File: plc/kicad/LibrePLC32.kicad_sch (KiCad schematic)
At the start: 0 parts

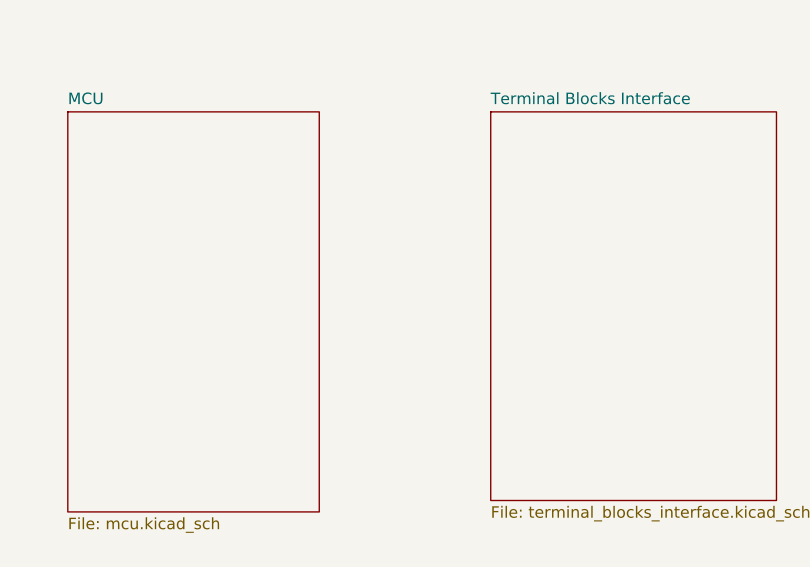
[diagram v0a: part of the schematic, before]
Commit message: Added gpio multiplexer and relay circuit
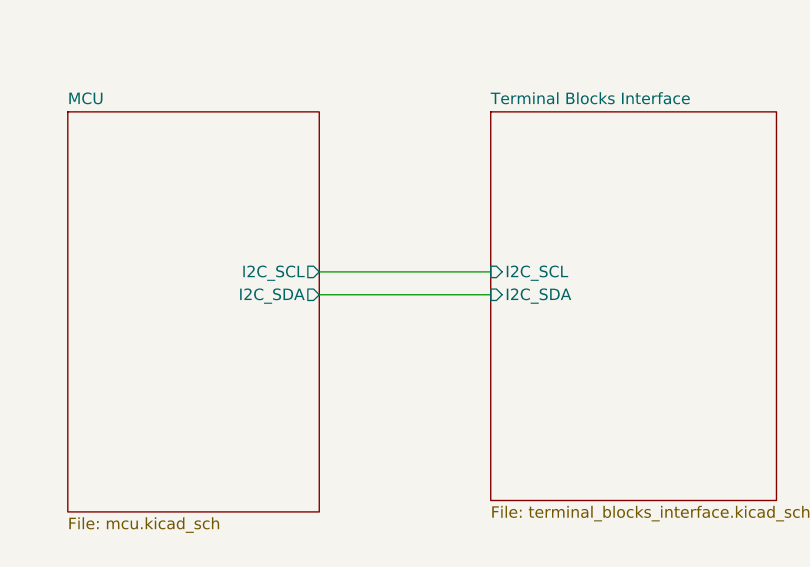
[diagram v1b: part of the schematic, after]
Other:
- sheet MCU ports: added I2C_SCL, I2C_SDA; removed none
- sheet Terminal Blocks Interface ports: added I2C_SCL, I2C_SDA; removed none
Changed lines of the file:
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@@
 	(generator_version "10.0")
 	(paper "A4")
+	(wire
+		(pts
+			(xy 154.94 90.17) (xy 173.99 90.17)
+		)
+		(stroke
+			(width 0)
+			(type default)
+		)
+	)
+	(wire
+		(pts
+			(xy 154.94 87.63) (xy 173.99 87.63)
+		)
+		(stroke
+			(width 0)
+			(type default)
+		)
+	)
 	(sheet
 		(at 50.8 74.93)
@@
 			)
 		)
+		(pin "I2C_SDA" input
+			(at 173.99 90.17 180)
+			(effects
+				(font
+					(size 1.27 1.27)
+				)
+				(justify left)
+			)
+		)
+		(pin "I2C_SCL" input
+			(at 173.99 87.63 180)
+			(effects
+				(font
+					(size 1.27 1.27)
+				)
+				(justify left)
+			)
+		)
 		(instances
 			(project "LibrePLC32"
@@
 			)
 		)
+		(pin "I2C_SDA" output
+			(at 154.94 90.17 0)
+			(effects
+				(font
+					(size 1.27 1.27)
+				)
+				(justify right)
+			)
+		)
+		(pin "I2C_SCL" output
+			(at 154.94 87.63 0)
+			(effects
+				(font
+					(size 1.27 1.27)
+				)
+				(justify right)
+			)
+		)

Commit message: Updated ethernet circuit
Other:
- sheet Ethernet ports: added ETH_MISO, ETH_MOSI, ETH_SCLK, ~{ETH_CS}, ~{ETH_INT}, ~{ETH_RST}; removed none
- sheet MCU ports: added ADC_RDY, ETH_MISO, ETH_MOSI, ETH_SCLK, MCU_DI, ~{ETH_CS}, ~{ETH_INT}, ~{ETH_RST}, ~{MUX_INT}; removed none
- sheet Terminal Blocks Interface ports: added ADC_RDY, MCU_DI, ~{MUX_INT}; removed none

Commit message: Added RS 485 circuit
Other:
- sheet MCU ports: added RS485_DIR, RS485_RXD, RS485_TXD; removed none
- sheet RS-485 ports: added RS485_DIR, RS485_RXD, RS485_TXD; removed none
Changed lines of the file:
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@@
+	(wire
+		(pts
+			(xy 127 102.235) (xy 82.55 102.235)
+		)
+		(stroke
+			(width 0)
+			(type default)
+		)
+	)
 	(wire
 		(pts
@@
 	(wire
 		(pts
+			(xy 82.55 104.775) (xy 127 104.775)
+		)
+		(stroke
+			(width 0)
+			(type default)
+		)
+	)
+	(wire
+		(pts
 			(xy 218.44 102.235) (xy 178.435 102.235)
+		)
+		(stroke
+			(width 0)
+			(type default)
+		)
+	)
+	(wire
+		(pts
+			(xy 82.55 107.315) (xy 127 107.315)
 		)
 		(stroke
@@
 	)
 	(sheet
-		(at 50.8 99.06)
-		(size 31.75 12.7)
+		(at 50.8 97.79)
+		(size 31.75 14.605)
 		(exclude_from_sim no)
 		(in_bom yes)
@@
 		)
 		(property "Sheetname" "RS-485"
-			(at 50.8 98.3484 0)
+			(at 50.8 97.0784 0)
 			(show_name no)
 			(do_not_autoplace no)
@@
 		)
 		(property "Sheetfile" "rs-485.kicad_sch"
-			(at 50.8 112.3446 0)
+			(at 50.8 112.9796 0)
 			(show_name no)
 			(do_not_autoplace no)
@@
 				)
 				(justify left top)
+			)
+		)
+		(pin "RS485_DIR" input
+			(at 82.55 102.235 0)
+			(effects
+				(font
+					(size 1.27 1.27)
+				)
+				(justify right)
+			)
+		)
+		(pin "RS485_RXD" bidirectional
+			(at 82.55 104.775 0)
+			(effects
+				(font
+					(size 1.27 1.27)
+				)
+				(justify right)
+			)
+		)
+		(pin "RS485_TXD" bidirectional
+			(at 82.55 107.315 0)
+			(effects
+				(font
+					(size 1.27 1.27)
+				)
+				(justify right)
 			)
 		)
@@
 			(effects
 				(font
+					(size 1.27 1.27)
+				)
+				(justify left)
+			)
+		)
+		(pin "RS485_DIR" output
+			(at 127 102.235 180)
+			(effects
+				(font
+					(size 1.27 1.27)
+				)
+				(justify left)
+			)
+		)
+		(pin "RS485_RXD" bidirectional
+			(at 127 104.775 180)
+			(effects
+				(font
+					(size 1.27 1.27)
+				)
+				(justify left)
+			)
+		)
+		(pin "RS485_TXD" bidirectional
+			(at 127 107.315 180)
+			(effects
+				(font

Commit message: Added CAN circuit
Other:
- sheet CAN ports: added CAN_FAULT, CAN_RX, CAN_TX; removed none
- sheet MCU ports: added CAN_FAULT, CAN_RX, CAN_TX; removed none
- title: (none) -> LibrePLC32
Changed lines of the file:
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@@
 	(generator_version "10.0")
 	(paper "A4")
+	(title_block
+		(title "LibrePLC32")
+	)
 	(polyline
 		(pts
@@
 	(wire
 		(pts
+			(xy 127 79.375) (xy 82.55 79.375)
+		)
+		(stroke
+			(width 0)
+			(type default)
+		)
+	)
+	(wire
+		(pts
 			(xy 127 102.235) (xy 82.55 102.235)
 		)
@@
 	(wire
 		(pts
+			(xy 82.55 84.455) (xy 127 84.455)
+		)
+		(stroke
+			(width 0)
+			(type default)
+		)
+	)
+	(wire
+		(pts
 			(xy 127 129.54) (xy 82.55 129.54)
 		)
@@
 		(pts
 			(xy 178.435 90.805) (xy 218.44 90.805)
+		)
+		(stroke
+			(width 0)
+			(type default)
+		)
+	)
+	(wire
+		(pts
+			(xy 127 81.915) (xy 82.55 81.915)
 		)
 		(stroke
@@
 			)
 		)
+		(pin "CAN_FAULT" output
+			(at 82.55 84.455 0)
+			(effects
+				(font
+					(size 1.27 1.27)
+				)
+				(justify right)
+			)
+		)
+		(pin "CAN_RX" output
+			(at 82.55 79.375 0)
+			(effects
+				(font
+					(size 1.27 1.27)
+				)
+				(justify right)
+			)
+		)
+		(pin "CAN_TX" input
+			(at 82.55 81.915 0)
+			(effects
+				(font
+					(size 1.27 1.27)
+				)
+				(justify right)
+			)
+		)
 		(instances
 			(project "LibrePLC32"
@@
 			(effects
 				(font
+					(size 1.27 1.27)
+				)
+				(justify left)
+			)
+		)
+		(pin "CAN_FAULT" input
+			(at 127 84.455 180)
+			(effects
+				(font
+					(size 1.27 1.27)
+				)
+				(justify left)
+			)
+		)
+		(pin "CAN_TX" output
+			(at 127 81.915 180)
+			(effects
+				(font
+					(size 1.27 1.27)
+				)
+				(justify left)
+			)
+		)
+		(pin "CAN_RX" input
+			(at 127 79.375 180)
+			(effects
+				(font

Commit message: Added the power protection IC
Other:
- sheet Power ports: added PPIC_IMON; removed none
- sheet Terminal Blocks Interface ports: added PPIC_IMON; removed none
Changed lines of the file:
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@@
+	(wire
+		(pts
+			(xy 82.55 52.07) (xy 89.535 52.07)
+		)
+		(stroke
+			(width 0)
+			(type default)
+		)
+	)
 	(wire
 		(pts
@@
 		)
 	)
+	(wire
+		(pts
+			(xy 89.535 34.29) (xy 212.09 34.29)
+		)
+		(stroke
+			(width 0)
+			(type default)
+		)
+	)
 	(polyline
 		(pts
@@
 		)
 	)
+	(wire
+		(pts
+			(xy 89.535 52.07) (xy 89.535 34.29)
+		)
+		(stroke
+			(width 0)
+			(type default)
+		)
+	)
 	(polyline
 		(pts
@@
 	(wire
 		(pts
+			(xy 212.09 34.29) (xy 212.09 77.47)
+		)
+		(stroke
+			(width 0)
+			(type default)
+		)
+	)
+	(wire
+		(pts
 			(xy 127 81.915) (xy 82.55 81.915)
 		)
@@
 			(width -0.0001)
 			(type solid)
+		)
+	)
+	(wire
+		(pts
+			(xy 212.09 77.47) (xy 218.44 77.47)
+		)
+		(stroke
+			(width 0)
+			(type default)
 		)
 	)
@@
 			)
 		)
+		(pin "PPIC_IMON" input
+			(at 218.44 77.47 180)
+			(effects
+				(font
+					(size 1.27 1.27)
+				)
+				(justify left)
+			)
+		)
 		(instances
 			(project "LibrePLC32"
@@
 			)
 		)
+		(pin "PPIC_IMON" output
+			(at 82.55 52.07 0)
+			(effects
+				(font
+					(size 1.27 1.27)
+				)
+				(justify right)
+			)
+		)

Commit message: Wired ESP32-S3 preliminarily
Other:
- sheet Power ports: added V_IN_MAIN; removed none
- sheet Terminal Blocks Interface ports: added V_IN_MAIN; removed none
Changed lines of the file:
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@@
-	(wire
-		(pts
-			(xy 82.55 52.07) (xy 89.535 52.07)
-		)
-		(stroke
-			(width 0)
-			(type default)
-		)
-	)
 	(wire
 		(pts
@@
 		)
 	)
-	(polyline
-		(pts
-			(xy 151848.5687 -151848.5687) (xy 151848.5687 -151848.5687)
-		)
-		(stroke
-			(width -0.0001)
-			(type solid)
+	(wire
+		(pts
+			(xy 209.55 56.515) (xy 209.55 80.01)
+		)
+		(stroke
+			(width 0)
+			(type default)
+		)
+	)
+	(polyline
+		(pts
+			(xy 151848.5687 -151848.5687) (xy 151848.5687 -151848.5687)
+		)
+		(stroke
+			(width -0.0001)
+			(type solid)
+		)
+	)
+	(wire
+		(pts
+			(xy 212.09 59.69) (xy 218.44 59.69)
+		)
+		(stroke
+			(width 0)
+			(type default)
 		)
 	)
@@
 		)
 	)
+	(wire
+		(pts
+			(xy 218.44 80.01) (xy 209.55 80.01)
+		)
+		(stroke
+			(width 0)
+			(type default)
+		)
+	)
 	(polyline
 		(pts
@@
 		)
 	)
-	(wire
-		(pts
-			(xy 89.535 34.29) (xy 212.09 34.29)
-		)
-		(stroke
-			(width 0)
-			(type default)
-		)
-	)
 	(polyline
 		(pts
@@
 		)
 	)
-	(wire
-		(pts
-			(xy 89.535 52.07) (xy 89.535 34.29)
-		)
-		(stroke
-			(width 0)
-			(type default)
-		)
-	)
 	(polyline
 		(pts
@@
 	(wire
 		(pts
-			(xy 212.09 34.29) (xy 212.09 77.47)
-		)
-		(stroke
-			(width 0)
-			(type default)
-		)
-	)
-	(wire
-		(pts
 			(xy 127 81.915) (xy 82.55 81.915)
 		)
@@
 		(pts
 			(xy 82.55 140.97) (xy 127 140.97)
+		)
+		(stroke
+			(width 0)
+			(type default)
+		)
+	)
+	(wire
+		(pts
+			(xy 212.09 77.47) (xy 212.09 59.69)
+		)
+		(stroke
+			(width 0)
+			(type default)
+		)
+	)
+	(wire
+		(pts
+			(xy 218.44 56.515) (xy 209.55 56.515)
 		)
 		(stroke
@@
 			)
 		)
+		(pin "V_IN_MAIN" output
+			(at 218.44 80.01 180)
+			(effects
+				(font
+					(size 1.27 1.27)
+				)
+				(justify left)
+			)
+		)
 		(instances
 			(project "LibrePLC32"
@@
 	)
 	(sheet
-		(at 50.8 49.53)
+		(at 218.44 48.26)
 		(size 31.75 13.97)
 		(exclude_from_sim no)
@@
 		)
 		(property "Sheetname" "Power"
-			(at 50.8 48.8184 0)
+			(at 218.44 47.5484 0)
 			(show_name no)
 			(do_not_autoplace no)
@@
 		)
 		(property "Sheetfile" "power.kicad_sch"
-			(at 50.8 64.0846 0)
+			(at 218.44 62.8146 0)
 			(show_name no)
 			(do_not_autoplace no)
@@
 		)
 		(pin "PPIC_IMON" output
-			(at 82.55 52.07 0)
-			(effects
-				(font
-					(size 1.27 1.27)
-				)
-				(justify right)
-			)
-		)
+			(at 218.44 59.69 180)
+			(effects
+				(font
+					(size 1.27 1.27)
+				)
+				(justify left)
+			)
+		)
+		(pin "V_IN_MAIN" input
+			(at 218.44 56.515 180)
+			(effects
+				(font
+					(size 1.27 1.27)
+				)
+				(justify left)
+			)
+		)

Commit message: PCB placement
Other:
- note added: "LibrePLC32"
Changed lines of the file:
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@@
 	(title_block
 		(title "LibrePLC32")
+		(date "2026-04-12")
+		(rev "A")
+	)
+	(text "LibrePLC32"
+		(exclude_from_sim no)
+		(at 201.93 173.99 0)
+		(effects
+			(font
+				(size 5 5)
+				(thickness 1)
+				(bold yes)
+				(color 72 0 0 1)
+			)
+		)
 	)
 	(polyline
